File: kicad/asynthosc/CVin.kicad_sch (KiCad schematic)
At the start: 12 parts, among them J2 AudioJack2, SW1 ${SIM.PARAMS}, U3 MCP6004

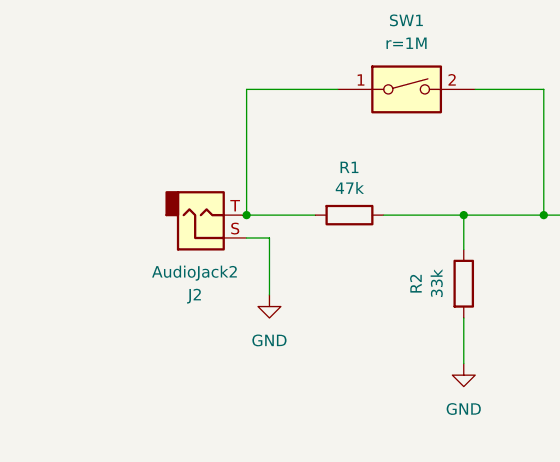
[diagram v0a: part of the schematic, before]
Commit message: sch: add spi nor, display connection, and more footprints
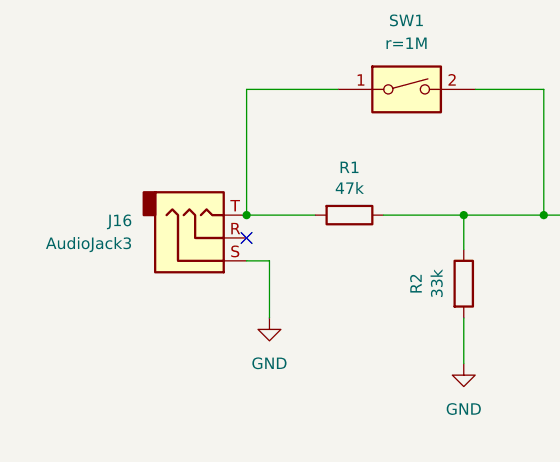
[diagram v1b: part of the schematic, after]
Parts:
- removed J2: AudioJack2, symbol Connector_Audio:AudioJack2
- added J16: AudioJack3, symbol Connector_Audio:AudioJack3
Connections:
- net GND: now also J16.S
- net at R1.2, SW1.1: now also J16.T
- no-connect marks 0 -> 1
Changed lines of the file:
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@@
+	)
+	(junction
+		(at 44.45 52.07)
+		(diameter 0)
+		(color 0 0 0 0)
 	)
 	(junction
@@
 		(color 0 0 0 0)
 	)
-	(junction
-		(at 44.45 52.07)
-		(diameter 0)
-		(color 0 0 0 0)
+	(no_connect
+		(at 44.45 54.61)
 	)
 	(wire
@@
 	(wire
 		(pts
-			(xy 46.99 54.61) (xy 44.45 54.61)
+			(xy 46.99 57.15) (xy 44.45 57.15)
 		)
 		(stroke
@@
 	(wire
 		(pts
-			(xy 46.99 54.61) (xy 46.99 60.96)
+			(xy 46.99 57.15) (xy 46.99 63.5)
 		)
 		(stroke
@@
 	)
 	(symbol
+		(lib_id "Connector_Audio:AudioJack3")
+		(at 39.37 54.61 0)
+		(mirror x)
+		(unit 1)
+		(exclude_from_sim no)
+		(in_bom yes)
+		(on_board yes)
+		(dnp no)
+		(property "Reference" "J16"
+			(at 31.75 52.7049 0)
+			(effects
+				(font
+					(size 1.27 1.27)
+				)
+				(justify right)
+			)
+		)
+		(property "Value" "AudioJack3"
+			(at 31.75 55.2449 0)
+			(effects
+				(font
+					(size 1.27 1.27)
+				)
+				(justify right)
+			)
+		)
+		(property "Footprint" ""
+			(at 39.37 54.61 0)
+			(effects
+				(font
+					(size 1.27 1.27)
+				)
+				(hide yes)
+			)
+		)
+		(property "Datasheet" "~"
+			(at 39.37 54.61 0)
+			(effects
+				(font
+					(size 1.27 1.27)
+				)
+				(hide yes)
+			)
+		)
+		(property "Description" "Audio Jack, 3 Poles (Stereo / TRS)"
+			(at 39.37 54.61 0)
+			(effects
+				(font
+					(size 1.27 1.27)
+				)
+				(hide yes)
+			)
+		)
+		(property "Sim.Device" "V"
+			(at 39.37 54.61 0)
+			(effects
+				(font
+					(size 1.27 1.27)
+				)
+				(hide yes)
+			)
+		)
+		(property "Sim.Type" "SIN"
+			(at 39.37 54.61 0)
+			(effects
+				(font
+					(size 1.27 1.27)
+				)
+				(hide yes)
+			)
+		)
+		(property "Sim.Pins" "S=- T=+"
+			(at 39.37 54.61 0)
+			(effects
+				(font
+					(size 1.27 1.27)
+				)
+				(hide yes)
+			)
+		)
+		(property "Sim.Params" "dc=0 ampl=12 f=2"
+			(at 39.37 54.61 0)
+			(effects
+				(font
+					(size 1.27 1.27)
+				)
+				(hide yes)
+			)
+		)
+		(pin "S"
+		)
+		(pin "R"
+		)
+		(pin "T"
+		)
+		(instances
+			(project "asynthosc"
+				(path "/d73e377a-a016-415f-8824-91cc6e4907b9/5f8430bb-1923-4d76-b418-f207310879ec/473ac791-b1b9-4029-b3bf-dcdd7bb809f7"
+					(reference "J16")
+					(unit 1)
+				)
+				(path "/d73e377a-a016-415f-8824-91cc6e4907b9/5f8430bb-1923-4d76-b418-f207310879ec/8df50db7-f715-4935-a0f9-d053a12e8abe"
+					(reference "J15")
+					(unit 1)
+				)
+				(path "/d73e377a-a016-415f-8824-91cc6e4907b9/5f8430bb-1923-4d76-b418-f207310879ec/9e63d1d7-077c-492b-8ed4-0ad38037f05a"
+					(reference "J14")
+					(unit 1)
+				)
+				(path "/d73e377a-a016-415f-8824-91cc6e4907b9/5f8430bb-1923-4d76-b418-f207310879ec/cf6627bb-bd84-4d9e-b011-633f72ceae80"
+					(reference "J7")
+					(unit 1)
+				)
+			)
+		)
+	)
+	(symbol
 		(lib_id "Switch:SW_DIP_x01")
 		(at 62.23 38.1 0)
@@
 				(path "/d73e377a-a016-415f-8824-91cc6e4907b9/5f8430bb-1923-4d76-b418-f207310879ec/cf6627bb-bd84-4d9e-b011-633f72ceae80"
 					(reference "SW5")
-					(unit 1)
-				)
-			)
-		)
-	)
-	(symbol
-		(lib_id "Connector_Audio:AudioJack2")
-		(at 39.37 52.07 0)
-		(mirror x)
-		(unit 1)
-		(exclude_from_sim no)
-		(in_bom yes)
-		(on_board yes)
-		(dnp no)
-		(property "Reference" "J2"
-			(at 38.735 60.96 0)
-			(effects
-				(font
-					(size 1.27 1.27)
-				)
-			)
-		)
-		(property "Value" "AudioJack2"
-			(at 38.735 58.42 0)
-			(effects
-				(font
-					(size 1.27 1.27)
-				)
-			)
-		)
-		(property "Footprint" ""
-			(at 39.37 52.07 0)
-			(effects
-				(font
-					(size 1.27 1.27)
-				)
-				(hide yes)
-			)
-		)
-		(property "Datasheet" "~"
-			(at 39.37 52.07 0)
-			(effects
-				(font
-					(size 1.27 1.27)
-				)
-				(hide yes)
-			)
-		)
-		(property "Description" "Audio Jack, 2 Poles (Mono / TS)"
-			(at 39.37 52.07 0)
-			(effects
-				(font
-					(size 1.27 1.27)
-				)
-				(hide yes)
-			)
-		)
-		(property "Sim.Device" "V"
-			(at 39.37 52.07 0)
-			(effects
-				(font
-					(size 1.27 1.27)
-				)
-				(hide yes)
-			)
-		)
-		(property "Sim.Type" "SIN"
-			(at 39.37 52.07 0)
-			(effects
-				(font
-					(size 1.27 1.27)
-				)
-				(hide yes)
-			)
-		)
-		(property "Sim.Pins" "S=- T=+"
-			(at 39.37 52.07 0)
-			(effects
-				(font
-					(size 1.27 1.27)
-				)
-				(hide yes)
-			)
-		)
-		(property "Sim.Params" "dc=0 ampl=12 f=1 td=0 theta=0 phase=0"
-			(at 39.37 52.07 0)
-			(effects
-				(font
-					(size 1.27 1.27)
-				)
-				(hide yes)
-			)
-		)
-		(pin "S"
-		)
-		(pin "T"
-		)
-		(instances
-			(project "asynthosc"
-				(path "/d73e377a-a016-415f-8824-91cc6e4907b9/5f8430bb-1923-4d76-b418-f207310879ec/473ac791-b1b9-4029-b3bf-dcdd7bb809f7"
-					(reference "J2")
-					(unit 1)
-				)
-				(path "/d73e377a-a016-415f-8824-91cc6e4907b9/5f8430bb-1923-4d76-b418-f207310879ec/8df50db7-f715-4935-a0f9-d053a12e8abe"
-					(reference "J10")
-					(unit 1)
-				)
-				(path "/d73e377a-a016-415f-8824-91cc6e4907b9/5f8430bb-1923-4d76-b418-f207310879ec/9e63d1d7-077c-492b-8ed4-0ad38037f05a"
-					(reference "J8")
-					(unit 1)
-				)
-				(path "/d73e377a-a016-415f-8824-91cc6e4907b9/5f8430bb-1923-4d76-b418-f207310879ec/cf6627bb-bd84-4d9e-b011-633f72ceae80"
-					(reference "J7")
 					(unit 1)
 				)
@@
 	(symbol
 		(lib_id "power:GND")
-		(at 46.99 60.96 0)
+		(at 46.99 63.5 0)
 		(unit 1)
 		(exclude_from_sim no)
@@
 		(fields_autoplaced yes)
 		(property "Reference" "#PWR014"
-			(at 46.99 67.31 0)
+			(at 46.99 69.85 0)
 			(effects
 				(font
@@
 		)
 		(property "Value" "GND"
-			(at 46.99 66.04 0)
+			(at 46.99 68.58 0)
 			(effects
 				(font
@@
 		)
 		(property "Footprint" ""
-			(at 46.99 60.96 0)
+			(at 46.99 63.5 0)
 			(effects
 				(font
@@
 		)
 		(property "Datasheet" ""
-			(at 46.99 60.96 0)
+			(at 46.99 63.5 0)
 			(effects
 				(font
@@
 		)
 		(property "Description" "Power symbol creates a global label with name \"GND\" , ground"
-			(at 46.99 60.96 0)
-			(effects
-				(font
+			(at 46.99 63.5 0)
+			(effects
+				(font

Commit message: sch: update footprint links
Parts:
- D4, D5: footprint (none) -> Diode_SMD:D_SOD-123
- J16: footprint (none) -> asynthosc:Jack_3.5mm_3legs_XKB_PJ-3411_Vertical
- R1, R2, R3, R4, R5, R6: footprint Resistor_SMD:R_0603_1608Metric -> Resistor_SMD:R_0402_1005Metric
- U3: footprint (none) -> Package_SO:TSSOP-14_4.4x5mm_P0.65mm
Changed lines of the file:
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@@
 			)
 		)
-		(property "Footprint" "Resistor_SMD:R_0603_1608Metric"
+		(property "Footprint" "Resistor_SMD:R_0402_1005Metric"
 			(at 113.03 40.132 90)
 			(effects
@@
 			)
 		)
-		(property "Footprint" "Resistor_SMD:R_0603_1608Metric"
+		(property "Footprint" "Resistor_SMD:R_0402_1005Metric"
 			(at 55.88 50.292 90)
 			(effects
@@
 			)
 		)
-		(property "Footprint" ""
+		(property "Footprint" "Diode_SMD:D_SOD-123"
 			(at 137.16 60.96 0)
 			(effects
@@
 			)
 		)
-		(property "Footprint" ""
+		(property "Footprint" "asynthosc:Jack_3.5mm_3legs_XKB_PJ-3411_Vertical"
 			(at 39.37 54.61 0)
 			(effects
@@
 			)
 		)
-		(property "Footprint" ""
+		(property "Footprint" "Package_SO:TSSOP-14_4.4x5mm_P0.65mm"
 			(at 111.76 57.15 0)
 			(effects
@@
 			)
 		)
-		(property "Footprint" "Resistor_SMD:R_0603_1608Metric"
+		(property "Footprint" "Resistor_SMD:R_0402_1005Metric"
 			(at 92.71 55.372 90)
 			(effects
@@
 			)
 		)
-		(property "Footprint" ""
+		(property "Footprint" "Diode_SMD:D_SOD-123"
 			(at 137.16 48.26 0)
 			(effects
@@
 			)
 		)
-		(property "Footprint" "Resistor_SMD:R_0603_1608Metric"
+		(property "Footprint" "Resistor_SMD:R_0402_1005Metric"
 			(at 66.802 59.69 90)
 			(effects
@@
 			)
 		)
-		(property "Footprint" "Resistor_SMD:R_0603_1608Metric"
+		(property "Footprint" "Resistor_SMD:R_0402_1005Metric"
 			(at 99.822 64.77 90)
 			(effects
@@
 			)
 		)
-		(property "Footprint" "Resistor_SMD:R_0603_1608Metric"
+		(property "Footprint" "Resistor_SMD:R_0402_1005Metric"
 			(at 87.63 50.292 90)
 			(effects

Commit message: sch: change stm32 for smaller one, create smaller jumper footprint
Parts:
- C6: RefNum (none) -> _generic_
- D4, D5: RefNum (none) -> 1N5817
- J16: Manufacturer (none) -> XKB; RefNum (none) -> PJ-3411
- U3: Manufacturer (none) -> Microchip; RefNum (none) -> MCP6004

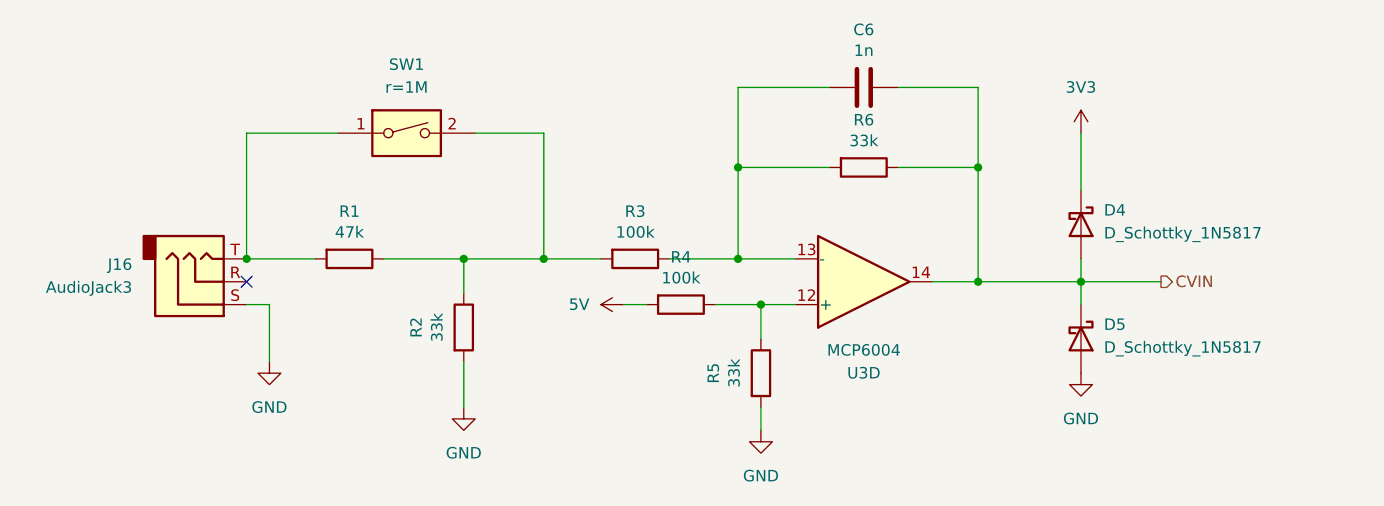
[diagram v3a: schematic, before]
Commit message: bom: update bom for lcsc
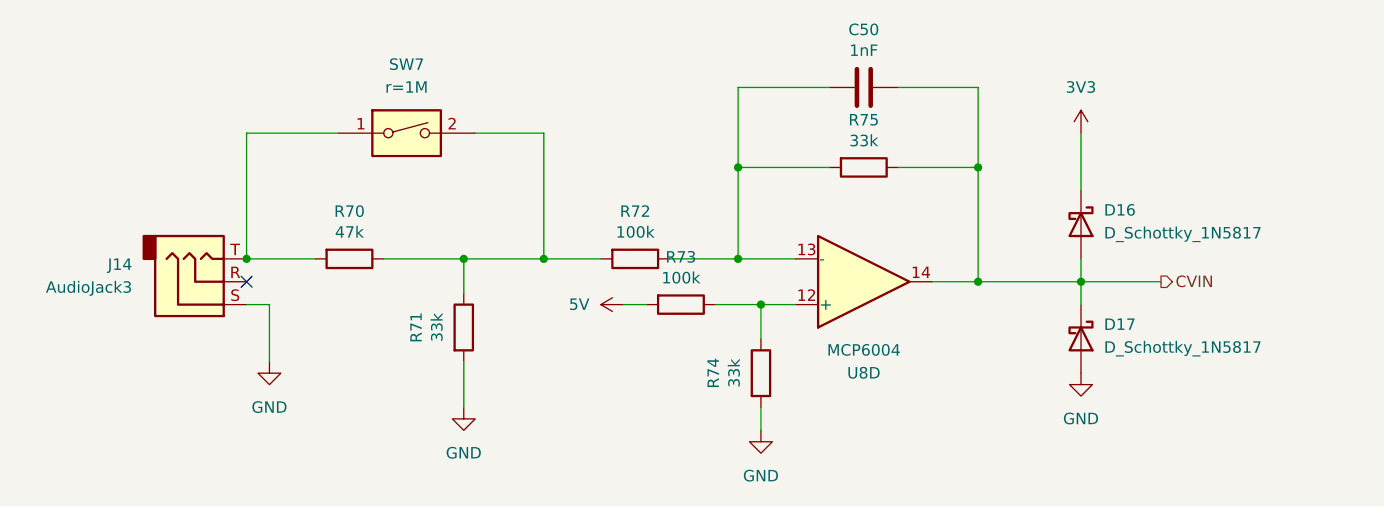
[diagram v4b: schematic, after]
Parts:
- C50: renamed from C6; value 1n -> 1nF
- R70: renamed from R1; RefNum (none) -> _generic_
- R71: renamed from R2; RefNum (none) -> _generic_
- R72: renamed from R3; RefNum (none) -> _generic_
- R73: renamed from R4; RefNum (none) -> _generic_
- R74: renamed from R5; RefNum (none) -> _generic_
- R75: renamed from R6; RefNum (none) -> _generic_
- U8: renamed from U3; RefNum MCP6004 -> MCP6004T-E/ST
- renumbered D4 to D16, D5 to D17, J16 to J14, SW1 to SW7

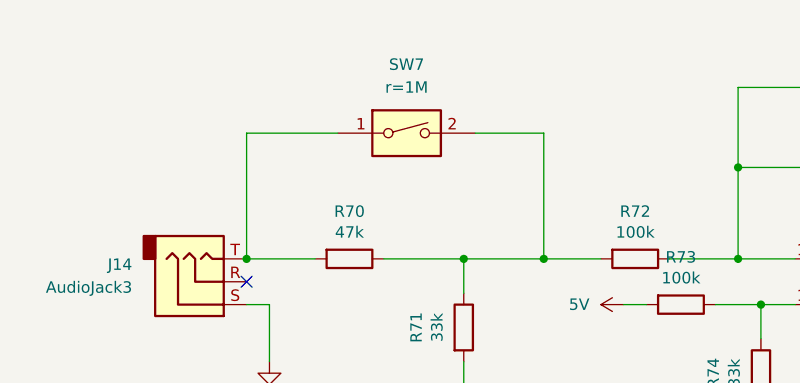
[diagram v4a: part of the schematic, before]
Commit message: sch: dip switch with separated sym
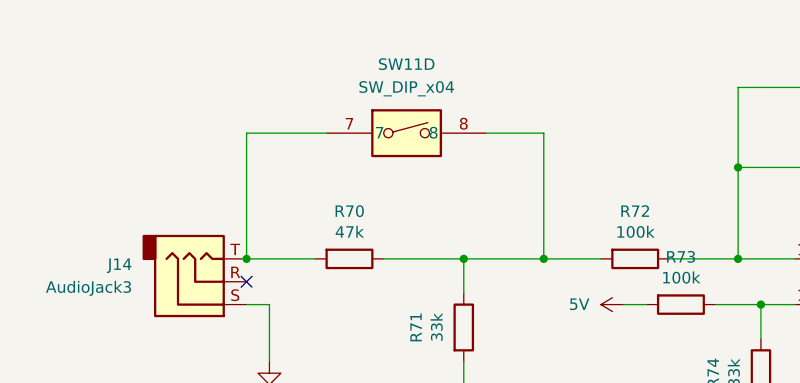
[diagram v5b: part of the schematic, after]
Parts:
- removed SW7: ${SIM.PARAMS}, symbol Switch:SW_DIP_x01
- added SW11: SW_DIP_x04, Button_Switch_SMD:SW_DIP_SPSTx04_Slide_6.7x11.72mm_W8.61mm_P2.54mm_LowProfile, symbol asynthosc_lib:SW_DIP_x04_SEP
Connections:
- net at R70.1, R71.1, R72.2: now also SW11.8
- net at J14.T, R70.2: now also SW11.7
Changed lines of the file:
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@@
 	(wire
 		(pts
-			(xy 44.45 38.1) (xy 54.61 38.1)
+			(xy 44.45 38.1) (xy 53.34 38.1)
 		)
 		(stroke
@@
 	(wire
 		(pts
-			(xy 146.05 54.61) (xy 137.16 54.61)
+			(xy 71.12 38.1) (xy 77.47 38.1)
 		)
 		(stroke
@@
 	(wire
 		(pts
-			(xy 69.85 38.1) (xy 77.47 38.1)
+			(xy 146.05 54.61) (xy 137.16 54.61)
 		)
 		(stroke
@@
 	)
 	(symbol
+		(lib_id "asynthosc_lib:SW_DIP_x04_SEP")
+		(at 62.23 38.1 0)
+		(unit 4)
+		(exclude_from_sim no)
+		(in_bom yes)
+		(on_board yes)
+		(dnp no)
+		(fields_autoplaced yes)
+		(property "Reference" "SW11"
+			(at 62.23 30.48 0)
+			(effects
+				(font
+					(size 1.27 1.27)
+				)
+			)
+		)
+		(property "Value" "SW_DIP_x04"
+			(at 62.23 33.02 0)
+			(effects
+				(font
+					(size 1.27 1.27)
+				)
+			)
+		)
+		(property "Footprint" "Button_Switch_SMD:SW_DIP_SPSTx04_Slide_6.7x11.72mm_W8.61mm_P2.54mm_LowProfile"
+			(at 62.23 38.1 0)
+			(effects
+				(font
+					(size 1.27 1.27)
+				)
+				(hide yes)
+			)
+		)
+		(property "Datasheet" ""
+			(at 62.23 38.1 0)
+			(effects
+				(font
+					(size 1.27 1.27)
+				)
+				(hide yes)
+			)
+		)
+		(property "Description" ""
+			(at 62.23 38.1 0)
+			(effects
+				(font
+					(size 1.27 1.27)
+				)
+				(hide yes)
+			)
+		)
+		(property "Manufacturer" "SM"
+			(at 62.23 38.1 0)
+			(effects
+				(font
+					(size 1.27 1.27)
+				)
+				(hide yes)
+			)
+		)
+		(property "RefNum" "  SMXS-04K-TP"
+			(at 62.23 38.1 0)
+			(effects
+				(font
+					(size 1.27 1.27)
+				)
+				(hide yes)
+			)
+		)
+		(pin "2"
+		)
+		(pin "1"
+		)
+		(pin "4"
+		)
+		(pin "3"
+		)
+		(pin "6"
+		)
+		(pin "7"
+		)
+		(pin "8"
+		)
+		(pin "5"
+		)
+		(instances
+			(project ""
+				(path "/d73e377a-a016-415f-8824-91cc6e4907b9/5f8430bb-1923-4d76-b418-f207310879ec/473ac791-b1b9-4029-b3bf-dcdd7bb809f7"
+					(reference "SW11")
+					(unit 4)
+				)
+				(path "/d73e377a-a016-415f-8824-91cc6e4907b9/5f8430bb-1923-4d76-b418-f207310879ec/8df50db7-f715-4935-a0f9-d053a12e8abe"
+					(reference "SW11")
+					(unit 3)
+				)
+				(path "/d73e377a-a016-415f-8824-91cc6e4907b9/5f8430bb-1923-4d76-b418-f207310879ec/9e63d1d7-077c-492b-8ed4-0ad38037f05a"
+					(reference "SW11")
+					(unit 2)
+				)
+				(path "/d73e377a-a016-415f-8824-91cc6e4907b9/5f8430bb-1923-4d76-b418-f207310879ec/cf6627bb-bd84-4d9e-b011-633f72ceae80"
+					(reference "SW11")
+					(unit 1)
+				)
+			)
+		)
+	)
+	(symbol
 		(lib_id "power:+3V3")
 		(at 137.16 38.1 0)
@@
 					(unit 1)
 				)
-			)
-		)
-	)
-	(symbol
-		(lib_id "Switch:SW_DIP_x01")
-		(at 62.23 38.1 0)
-		(unit 1)
-		(exclude_from_sim no)
-		(in_bom yes)
-		(on_board yes)
-		(dnp no)
-		(fields_autoplaced yes)
-		(property "Reference" "SW7"
-			(at 62.23 30.48 0)
-			(effects
-				(font
-					(size 1.27 1.27)
-				)
-			)
-		)
-		(property "Value" "${SIM.PARAMS}"
-			(at 62.23 33.02 0)
-			(effects
-				(font
-					(size 1.27 1.27)
-				)
-			)
-		)
-		(property "Footprint" ""
-			(at 62.23 38.1 0)
-			(effects
-				(font
-					(size 1.27 1.27)
-				)
-				(hide yes)
-			)
-		)
-		(property "Datasheet" "~"
-			(at 62.23 38.1 0)
-			(effects
-				(font
-					(size 1.27 1.27)
-				)
-				(hide yes)
-			)
-		)
-		(property "Description" "1x DIP Switch, Single Pole Single Throw (SPST) switch, small symbol"
-			(at 62.23 38.1 0)
-			(effects
-				(font
-					(size 1.27 1.27)
-				)
-				(hide yes)
-			)
-		)
-		(property "Sim.Device" "R"
-			(at 62.23 38.1 0)
-			(effects
-				(font
-					(size 1.27 1.27)
-				)
-				(hide yes)
-			)
-		)
-		(property "Sim.Pins" "1=+ 2=-"
-			(at 62.23 38.1 0)
-			(effects
-				(font
-					(size 1.27 1.27)
-				)
-				(hide yes)
-			)
-		)
-		(property "Sim.Params" "r=1M"
-			(at 62.23 38.1 0)
-			(effects
-				(font
-					(size 1.27 1.27)
-				)
-				(hide yes)
-			)
-		)
-		(property "LCSC" ""
-			(at 62.23 38.1 0)
-			(effects
-				(font
-					(size 1.27 1.27)
-				)
-				(hide yes)
-			)
-		)
-		(property "Manufacturer" ""
-			(at 62.23 38.1 0)
-			(effects
-				(font
-					(size 1.27 1.27)
-				)
-				(hide yes)
-			)
-		)
-		(pin "2"
-		)
-		(pin "1"
-		)
-		(instances
-			(project "asynthosc"
-				(path "/d73e377a-a016-415f-8824-91cc6e4907b9/5f8430bb-1923-4d76-b418-f207310879ec/473ac791-b1b9-4029-b3bf-dcdd7bb809f7"
-					(reference "SW7")
-					(unit 1)
-				)
-				(path "/d73e377a-a016-415f-8824-91cc6e4907b9/5f8430bb-1923-4d76-b418-f207310879ec/8df50db7-f715-4935-a0f9-d053a12e8abe"
-					(reference "SW5")
-					(unit 1)
-				)
-				(path "/d73e377a-a016-415f-8824-91cc6e4907b9/5f8430bb-1923-4d76-b418-f207310879ec/9e63d1d7-077c-492b-8ed4-0ad38037f05a"
-					(reference "SW4")
-					(unit 1)
-				)
-				(path "/d73e377a-a016-415f-8824-91cc6e4907b9/5f8430bb-1923-4d76-b418-f207310879ec/cf6627bb-bd84-4d9e-b011-633f72ceae80"
-					(reference "SW3")
-					(unit 1)
-				)

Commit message: pcb: placing
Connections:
- net at R70.1, R71.1, R72.2: now also SW11.5 (2); no longer SW11.8
- net at J14.T, R70.2: now also SW11.4 (1); no longer SW11.7
